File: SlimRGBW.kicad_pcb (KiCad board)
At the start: 2 copper layers, 8 parts, among them J1 Conn_01x05_Pin, U1 ESP32-C3-MINI-1

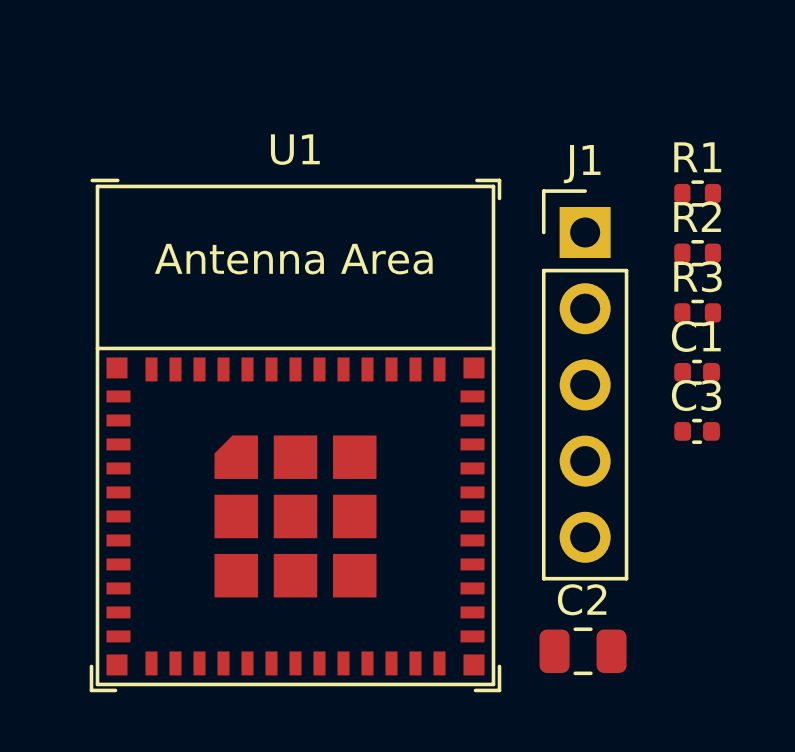
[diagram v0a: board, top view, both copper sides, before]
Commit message: Add mosfets to schematic, no footprint yet
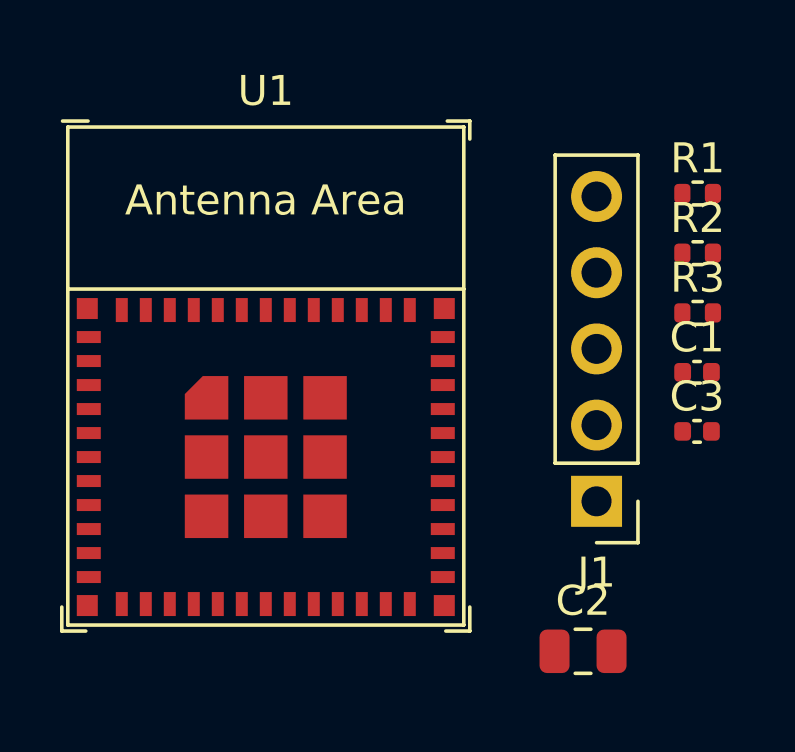
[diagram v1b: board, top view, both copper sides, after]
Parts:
- moved J1 8.97 mm to (157.0, 85.0), turned to 180 degrees
- moved U1 2.21 mm to (146.0, 80.8)
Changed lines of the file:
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@@
 	(footprint "Connector_PinHeader_2.54mm:PinHeader_1x05_P2.54mm_Vertical"
 		(layer "F.Cu")
-		(at 156.62 76.04)
+		(at 157 85 180)
 		(descr "Through hole straight pin header, 1x05, 2.54mm pitch, single row")
 		(tags "Through hole pin header THT 1x05 2.54mm single row")
@@
 		(attr through_hole)
 		(fp_line
+			(start 1.38 1.27)
+			(end 1.38 11.54)
+			(stroke
+				(width 0.12)
+				(type solid)
+			)
+			(layer "F.SilkS")
+		)
+		(fp_line
+			(start -1.38 11.54)
+			(end 1.38 11.54)
+			(stroke
+				(width 0.12)
+				(type solid)
+			)
+			(layer "F.SilkS")
+		)
+		(fp_line
+			(start -1.38 1.27)
+			(end 1.38 1.27)
+			(stroke
+				(width 0.12)
+				(type solid)
+			)
+			(layer "F.SilkS")
+		)
+		(fp_line
+			(start -1.38 1.27)
+			(end -1.38 11.54)
+			(stroke
+				(width 0.12)
+				(type solid)
+			)
+			(layer "F.SilkS")
+		)
+		(fp_line
+			(start -1.38 0)
+			(end -1.38 -1.38)
+			(stroke
+				(width 0.12)
+				(type solid)
+			)
+			(layer "F.SilkS")
+		)
+		(fp_line
 			(start -1.38 -1.38)
 			(end 0 -1.38)
@@
 		)
 		(fp_line
-			(start -1.38 0)
-			(end -1.38 -1.38)
-			(stroke
-				(width 0.12)
-				(type solid)
-			)
-			(layer "F.SilkS")
-		)
-		(fp_line
-			(start -1.38 1.27)
-			(end -1.38 11.54)
-			(stroke
-				(width 0.12)
-				(type solid)
-			)
-			(layer "F.SilkS")
-		)
-		(fp_line
-			(start -1.38 1.27)
-			(end 1.38 1.27)
-			(stroke
-				(width 0.12)
-				(type solid)
-			)
-			(layer "F.SilkS")
-		)
-		(fp_line
-			(start -1.38 11.54)
-			(end 1.38 11.54)
-			(stroke
-				(width 0.12)
-				(type solid)
-			)
-			(layer "F.SilkS")
-		)
-		(fp_line
-			(start 1.38 1.27)
-			(end 1.38 11.54)
-			(stroke
-				(width 0.12)
-				(type solid)
-			)
-			(layer "F.SilkS")
+			(start 1.77 11.93)
+			(end 1.77 -1.77)
+			(stroke
+				(width 0.05)
+				(type solid)
+			)
+			(layer "F.CrtYd")
+		)
+		(fp_line
+			(start 1.77 -1.77)
+			(end -1.77 -1.77)
+			(stroke
+				(width 0.05)
+				(type solid)
+			)
+			(layer "F.CrtYd")
+		)
+		(fp_line
+			(start -1.77 11.93)
+			(end 1.77 11.93)
+			(stroke
+				(width 0.05)
+				(type solid)
+			)
+			(layer "F.CrtYd")
 		)
 		(fp_line
@@
 		)
 		(fp_line
-			(start -1.77 11.93)
-			(end 1.77 11.93)
-			(stroke
-				(width 0.05)
-				(type solid)
-			)
-			(layer "F.CrtYd")
-		)
-		(fp_line
-			(start 1.77 -1.77)
-			(end -1.77 -1.77)
-			(stroke
-				(width 0.05)
-				(type solid)
-			)
-			(layer "F.CrtYd")
-		)
-		(fp_line
-			(start 1.77 11.93)
-			(end 1.77 -1.77)
-			(stroke
-				(width 0.05)
-				(type solid)
-			)
-			(layer "F.CrtYd")
+			(start 1.27 11.43)
+			(end -1.27 11.43)
+			(stroke
+				(width 0.1)
+				(type solid)
+			)
+			(layer "F.Fab")
+		)
+		(fp_line
+			(start 1.27 -1.27)
+			(end 1.27 11.43)
+			(stroke
+				(width 0.1)
+				(type solid)
+			)
+			(layer "F.Fab")
+		)
+		(fp_line
+			(start -0.635 -1.27)
+			(end 1.27 -1.27)
+			(stroke
+				(width 0.1)
+				(type solid)
+			)
+			(layer "F.Fab")
+		)
+		(fp_line
+			(start -1.27 11.43)
+			(end -1.27 -0.635)
+			(stroke
+				(width 0.1)
+				(type solid)
+			)
+			(layer "F.Fab")
 		)
 		(fp_line
@@
 			(layer "F.Fab")
 		)
-		(fp_line
-			(start -1.27 11.43)
-			(end -1.27 -0.635)
-			(stroke
-				(width 0.1)
-				(type solid)
-			)
-			(layer "F.Fab")
-		)
-		(fp_line
-			(start -0.635 -1.27)
-			(end 1.27 -1.27)
-			(stroke
-				(width 0.1)
-				(type solid)
-			)
-			(layer "F.Fab")
-		)
-		(fp_line
-			(start 1.27 -1.27)
-			(end 1.27 11.43)
-			(stroke
-				(width 0.1)
-				(type solid)
-			)
-			(layer "F.Fab")
-		)
-		(fp_line
-			(start 1.27 11.43)
-			(end -1.27 11.43)
-			(stroke
-				(width 0.1)
-				(type solid)
-			)
-			(layer "F.Fab")
-		)
 		(fp_text user "${REFERENCE}"
 			(at 0 5.08 90)
@@
 		)
 		(pad "1" thru_hole rect
-			(at 0 0)
+			(at 0 0 180)
 			(size 1.7 1.7)
 			(drill 1)
@@
 		)
 		(pad "2" thru_hole circle
-			(at 0 2.54)
+			(at 0 2.54 180)
 			(size 1.7 1.7)
 			(drill 1)
@@
 		)
 		(pad "3" thru_hole circle
-			(at 0 5.08)
+			(at 0 5.08 180)
 			(size 1.7 1.7)
 			(drill 1)
@@
 		)
 		(pad "4" thru_hole circle
-			(at 0 7.62)
+			(at 0 7.62 180)
 			(size 1.7 1.7)
 			(drill 1)
@@
 		)
 		(pad "5" thru_hole circle
-			(at 0 10.16)
+			(at 0 10.16 180)
 			(size 1.7 1.7)
 			(drill 1)
@@
 	(footprint "PCM_Espressif:ESP32-C3-MINI-1"
 		(layer "F.Cu")
-		(at 146.965 82.805)
+		(at 145.975 80.825)
 		(descr "ESP32-C3-MINI-1: https://www.espressif.com/sites/default/files/documentation/esp32-c3-mini-1_datasheet_en.pdf")
 		(tags "ESP32-C3")
@@
 			(polygon
 				(pts
-					(xy 153.565 79.905) (xy 140.365 79.905) (xy 140.365 74.505) (xy 153.565 74.505)
-				)
-			)
+					(xy 152.575 77.925) (xy 139.375 77.925) (xy 139.375 72.525) (xy 152.575 72.525)
+				)
+			)
